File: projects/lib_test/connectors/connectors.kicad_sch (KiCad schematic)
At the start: 0 parts

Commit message: updated lib test
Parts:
- added X1001: 1x02_PH, lily_footprints:con_jst_1x02_ph_2.00mm_right_angle_th, symbol lily_symbols:con_jst_1x02_PH_2.00mm_right_angle_th
- added X1002: 1x02_VH, lily_footprints:con_jst_1x02_vh_3.96mm_right_angle_th, symbol lily_symbols:con_jst_1x02_VH_3.96mm_right_angle_th
- added X1003: 1x02_PH, lily_footprints:con_jst_1x02_ph_2.00mm_straight_smd, symbol lily_symbols:con_jst_1x02_PH_2.00mm_straight_smd
- added X1004: 1x06_PH, lily_footprints:con_jst_1x06_ph_2.00mm_straight_smd, symbol lily_symbols:con_jst_1x06_PH_2.00mm_straight_smd
- added X1005: 1x07_PH, lily_footprints:con_jst_1x07_ph_2.00mm_straight_smd, symbol lily_symbols:con_jst_1x07_PH_2.00mm_straight_smd
- added X1006: 1x08_PH, lily_footprints:con_jst_1x08_ph_2.00mm_straight_smd, symbol lily_symbols:con_jst_1x08_PH_2.00mm_straight_smd
- added X1007: 1x06, lily_footprints:con_header_1x06_2.54mm_th, symbol lily_symbols:con_header_1x06_2.54mm_th
- added X1008: 1x10, lily_footprints:con_header_1x10_2.54mm_th, symbol lily_symbols:con_header_1x10_2.54mm_th
- added X1009: 2x03, lily_footprints:con_header_2x03_2.54mm_th, symbol lily_symbols:con_header_2x03_2.54mm_th
- added X1010: 1x04_PH, lily_footprints:con_jst_1x04_ph_2.00mm_right_angle_th, symbol lily_symbols:con_jst_1x04_PH_2.00mm_right_angle_th
- added X1011: 1x04_VH, lily_footprints:con_jst_1x04_vh_3.96mm_right_angle_th, symbol lily_symbols:con_jst_1x04_VH_3.96mm_right_angle_th
- added X1012: 1x04_PH, lily_footprints:con_jst_1x04_ph_2.00mm_straight_smd, symbol lily_symbols:con_jst_1x04_PH_2.00mm_straight_smd
- added X1013: 1x03_PH, lily_footprints:con_jst_1x03_ph_2.00mm_straight_smd, symbol lily_symbols:con_jst_1x03_PH_2.00mm_straight_smd
- added X1014: din41612_plug, lily_footprints:con_din41612_plug_64p_a+c_right_angle_th, symbol lily_symbols:con_din41612_plug_64p_a+c_right_angle_th
- added X1015: din41612_receptacle, lily_footprints:con_din41612_receptacle_64p_a+c_right_angle_th, symbol lily_symbols:con_din41612_receptacle_64p_a+c_right_angle_th
- added X1016: din41612_receptacle, lily_footprints:con_din41612_receptacle_64p_a+c_straight_th, symbol lily_symbols:con_din41612_receptacle_64p_a+c_straight_th
- added X1017: dc_005, lily_footprints:con_dc_jack_dc_005_th, symbol lily_symbols:con_dc_jack_dc_005_th
- added X1018: 1x15, lily_footprints:con_socket_1x15_2.54mm_straight_th, symbol lily_symbols:con_socket_1x15_2.54mm_straight_th
- added X1019: sub_d_hd_plug, lily_footprints:con_sub_d_hd_plug_44p_right_angle_th, symbol lily_symbols:con_sub_d_hd_plug_44p_th
- added X1020: sub_d_hd_receptacle, lily_footprints:con_sub_d_hd_receptacle_44p_right_angle_th, symbol lily_symbols:con_sub_d_hd_receptacle_44p_th
- added X1021: 2p_5.08, lily_footprints:con_terminal_block_2p_5.08mm_th, symbol lily_symbols:con_terminal_block_2p_5.08_th
- added X1022: 3p_5.08, lily_footprints:con_terminal_block_3p_5.08mm_th, symbol lily_symbols:con_terminal_block_3p_5.08_th
- added X1023: socket_male, lily_footprints:con_terminal_socket_male_10p_3.81mm_right_angle_th, symbol lily_symbols:con_terminal_socket_male_10p_3.81mm_right_angle_th
- added X1024: usb_b, lily_footprints:con_usb_b_receptacle_th, symbol lily_symbols:con_usb_b_receptacle_th
- added X1025: usb_c, lily_footprints:con_usb_c_receptacle_16p, symbol lily_symbols:con_usb_c_receptacle_16p
- added X1026: RCJ6A-H, lily_footprints:con_xlr_jack_rcj6fa-h_th, symbol lily_symbols:con_xlr_jack_7p_RCJ6A-H_th
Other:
- note added: "DIN41612"
- note added: "HEADERS AND SOCKETS"
- note added: "JST CONNECTORS"
- note added: "SUB-D"
- note added: "TERMINAL BLOCKS"
- note added: "VARIOUS"

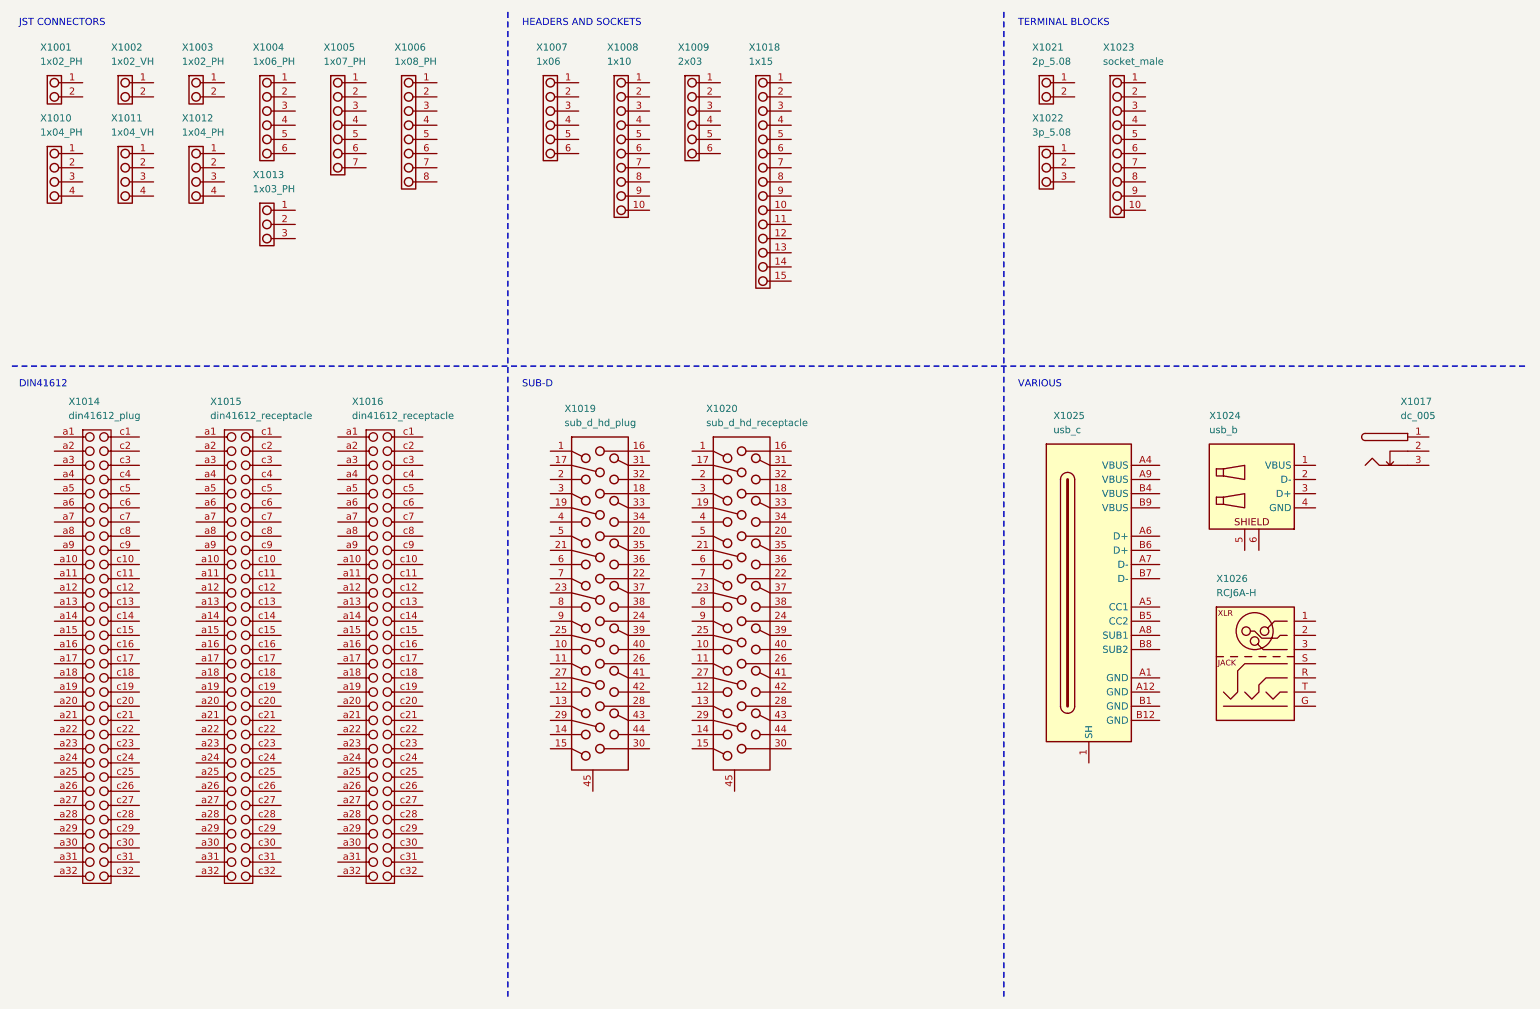
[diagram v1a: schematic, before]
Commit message: updated test project for connectors
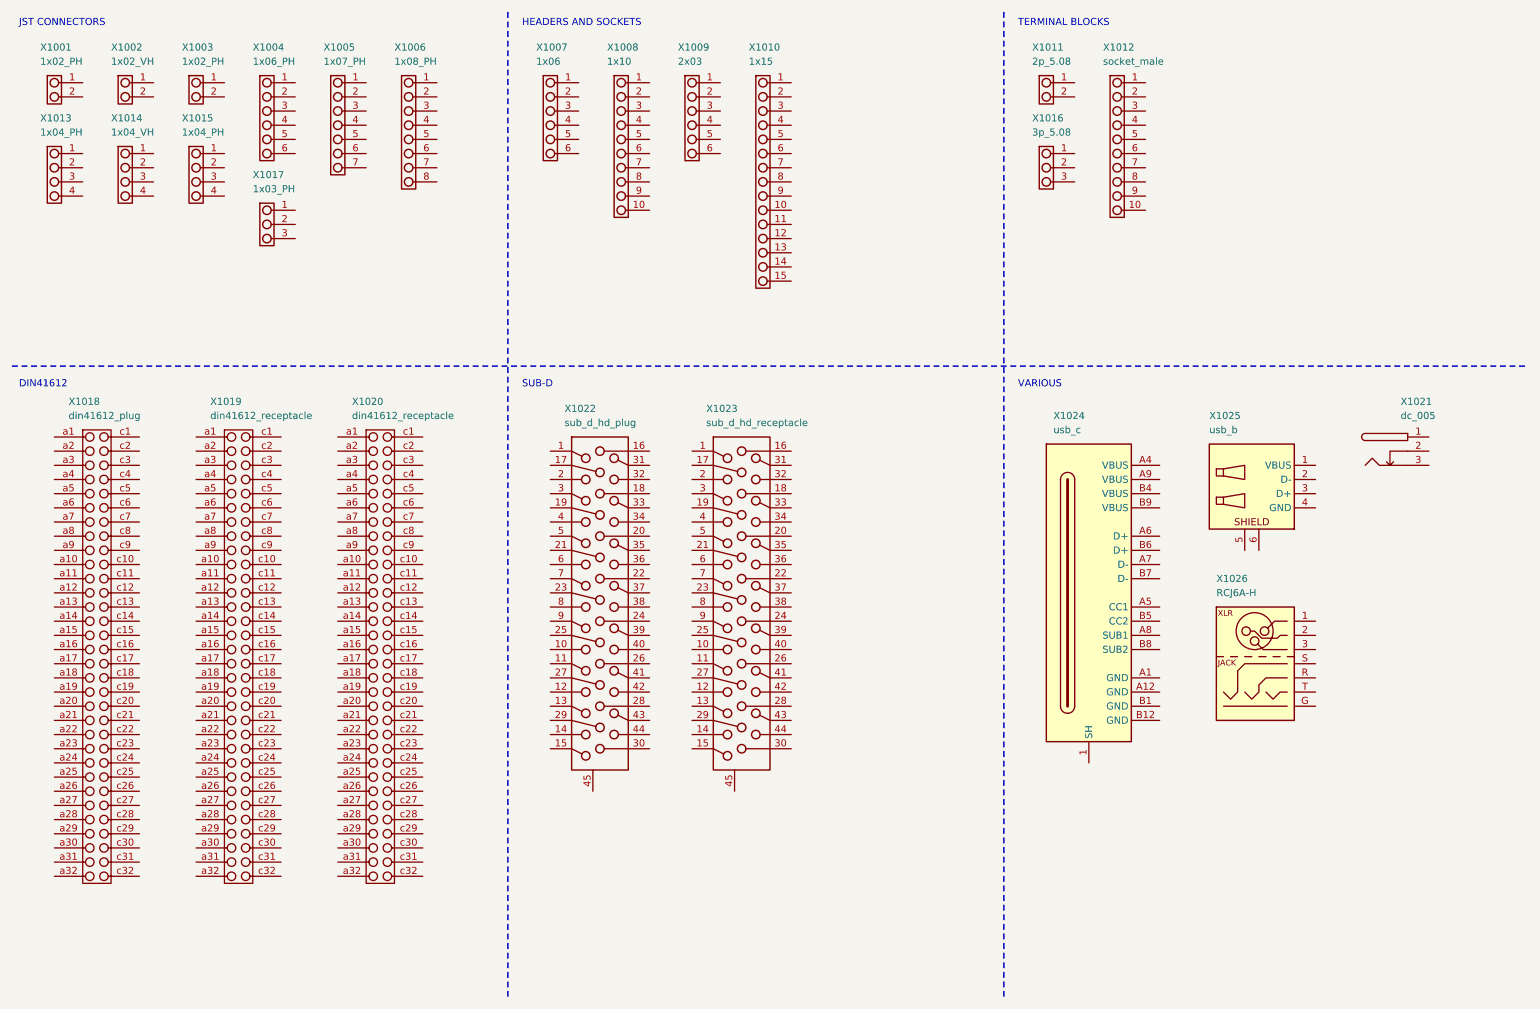
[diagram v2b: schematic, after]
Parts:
- renumbered X1018 to X1010, X1021 to X1011, X1023 to X1012, X1010 to X1013, X1011 to X1014, X1012 to X1015, X1022 to X1016, X1013 to X1017, X1014 to X1018, X1015 to X1019, X1016 to X1020, X1017 to X1021, X1019 to X1022, X1020 to X1023, X1025 to X1024, X1024 to X1025
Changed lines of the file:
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@@
 		(on_board yes)
 		(dnp no)
-		(property "Reference" "X1022"
+		(property "Reference" "X1016"
 			(at 195.58 31.75 0)
 			(effects
@@
 			(project ""
 				(path "/e63e39d7-6ac0-4ffd-8aa3-1841a4541b55"
-					(reference "X1022")
+					(reference "X1016")
 					(unit 1)
 				)
@@
 		(on_board yes)
 		(dnp no)
-		(property "Reference" "X1013"
+		(property "Reference" "X1017"
 			(at 55.88 41.91 0)
 			(effects
@@
 			(project ""
 				(path "/e63e39d7-6ac0-4ffd-8aa3-1841a4541b55"
-					(reference "X1013")
+					(reference "X1017")
 					(unit 1)
 				)
@@
 		(on_board yes)
 		(dnp no)
-		(property "Reference" "X1018"
+		(property "Reference" "X1010"
 			(at 144.78 19.05 0)
 			(effects
@@
 			(project ""
 				(path "/e63e39d7-6ac0-4ffd-8aa3-1841a4541b55"
-					(reference "X1018")
+					(reference "X1010")
 					(unit 1)
 				)
@@
 		(on_board yes)
 		(dnp no)
-		(property "Reference" "X1012"
+		(property "Reference" "X1015"
 			(at 43.18 31.75 0)
 			(effects
@@
 			(project ""
 				(path "/e63e39d7-6ac0-4ffd-8aa3-1841a4541b55"
-					(reference "X1012")
+					(reference "X1015")
 					(unit 1)
 				)
@@
 		(on_board yes)
 		(dnp no)
-		(property "Reference" "X1014"
+		(property "Reference" "X1018"
 			(at 22.86 82.55 0)
 			(effects
@@
 			(project ""
 				(path "/e63e39d7-6ac0-4ffd-8aa3-1841a4541b55"
-					(reference "X1014")
+					(reference "X1018")
 					(unit 1)
 				)
@@
 		(on_board yes)
 		(dnp no)
-		(property "Reference" "X1015"
+		(property "Reference" "X1019"
 			(at 48.26 82.55 0)
 			(effects
@@
 			(project ""
 				(path "/e63e39d7-6ac0-4ffd-8aa3-1841a4541b55"
-					(reference "X1015")
+					(reference "X1019")
 					(unit 1)
 				)
@@
 		(on_board yes)
 		(dnp no)
-		(property "Reference" "X1010"
+		(property "Reference" "X1013"
 			(at 17.78 31.75 0)
 			(effects
@@
 			(project ""
 				(path "/e63e39d7-6ac0-4ffd-8aa3-1841a4541b55"
-					(reference "X1010")
+					(reference "X1013")
 					(unit 1)
 				)
@@
 		(on_board yes)
 		(dnp no)
-		(property "Reference" "X1019"
+		(property "Reference" "X1022"
 			(at 111.76 83.82 0)
 			(effects
@@
 			(project ""
 				(path "/e63e39d7-6ac0-4ffd-8aa3-1841a4541b55"
-					(reference "X1019")
+					(reference "X1022")
 					(unit 1)
 				)
@@
 		(on_board yes)
 		(dnp no)
-		(property "Reference" "X1020"
+		(property "Reference" "X1023"
 			(at 137.16 83.82 0)
 			(effects
@@
 			(project ""
 				(path "/e63e39d7-6ac0-4ffd-8aa3-1841a4541b55"
-					(reference "X1020")
+					(reference "X1023")
 					(unit 1)
 				)
@@
 		(on_board yes)
 		(dnp no)
-		(property "Reference" "X1023"
+		(property "Reference" "X1012"
 			(at 208.28 19.05 0)
 			(effects
@@
 			(project ""
 				(path "/e63e39d7-6ac0-4ffd-8aa3-1841a4541b55"
-					(reference "X1023")
+					(reference "X1012")
 					(unit 1)
 				)
@@
 		(on_board yes)
 		(dnp no)
-		(property "Reference" "X1017"
+		(property "Reference" "X1021"
 			(at 261.62 82.55 0)
 			(effects
@@
 			(project ""
 				(path "/e63e39d7-6ac0-4ffd-8aa3-1841a4541b55"
-					(reference "X1017")
+					(reference "X1021")
 					(unit 1)
 				)
@@
 		(on_board yes)
 		(dnp no)
-		(property "Reference" "X1025"
+		(property "Reference" "X1024"
 			(at 199.39 85.09 0)
 			(effects
@@
 			(project ""
 				(path "/e63e39d7-6ac0-4ffd-8aa3-1841a4541b55"
-					(reference "X1025")
+					(reference "X1024")
 					(unit 1)
 				)
@@
 		(on_board yes)
 		(dnp no)
-		(property "Reference" "X1021"
+		(property "Reference" "X1011"
 			(at 195.58 19.05 0)
 			(effects
@@
 			(project ""
 				(path "/e63e39d7-6ac0-4ffd-8aa3-1841a4541b55"
-					(reference "X1021")
+					(reference "X1011")
 					(unit 1)
 				)
@@
 		(on_board yes)
 		(dnp no)
-		(property "Reference" "X1016"
+		(property "Reference" "X1020"
 			(at 73.66 82.55 0)
 			(effects
@@
 			(project ""
 				(path "/e63e39d7-6ac0-4ffd-8aa3-1841a4541b55"
-					(reference "X1016")
+					(reference "X1020")
 					(unit 1)
 				)
@@
 		(on_board yes)
 		(dnp no)
-		(property "Reference" "X1024"
+		(property "Reference" "X1025"
 			(at 227.33 85.09 0)
 			(effects
@@
 			(project ""
 				(path "/e63e39d7-6ac0-4ffd-8aa3-1841a4541b55"
-					(reference "X1024")
+					(reference "X1025")
 					(unit 1)
 				)
@@
 		(on_board yes)
 		(dnp no)
-		(property "Reference" "X1011"
+		(property "Reference" "X1014"
 			(at 30.48 31.75 0)
 			(effects
@@
 			(project ""
 				(path "/e63e39d7-6ac0-4ffd-8aa3-1841a4541b55"
-					(reference "X1011")
+					(reference "X1014")
 					(unit 1)
 				)

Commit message: updated test projects
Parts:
- added X1015: 1x03_PH, lily_footprints:con_jst_1x03_ph_2.00mm_right_angle_th, symbol lily_symbols:con_jst_1x03_PH_2.00mm_right_angle_th
- added X1027: SMA, lily_footprints:con_rf_sma_right_angle_th, symbol lily_symbols:con_rf_sma_right_angle_th
- added X1029: TC2030-IDC, lily_footprints:con_tc2030_idc_lock, symbol lily_symbols:con_TC2030-IDC_lock
- renumbered X1016 to X1013, X1017 to X1014, X1013 to X1016, X1014 to X1017, X1015 to X1018, X1018 to X1019, X1019 to X1020, X1020 to X1021, X1021 to X1022, X1022 to X1023, X1023 to X1024, X1024 to X1025, X1025 to X1026, X1026 to X1028
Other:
- moved on the sheet: X1014, X1016, X1017, X1018
